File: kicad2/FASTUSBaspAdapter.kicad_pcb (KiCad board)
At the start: 2 copper layers, 73.7 x 29.2 mm, 2 parts, among them CON1 AVR-ISP-6, U1 stm32f103c8t6-module-china

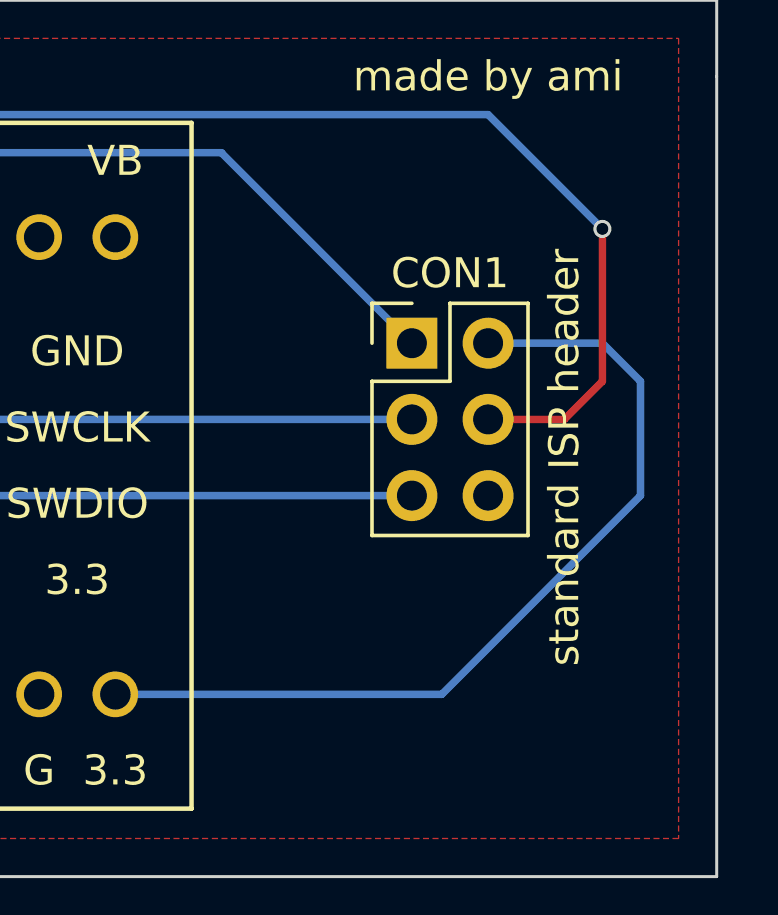
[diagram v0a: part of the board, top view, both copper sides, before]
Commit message: Add panelize pcb
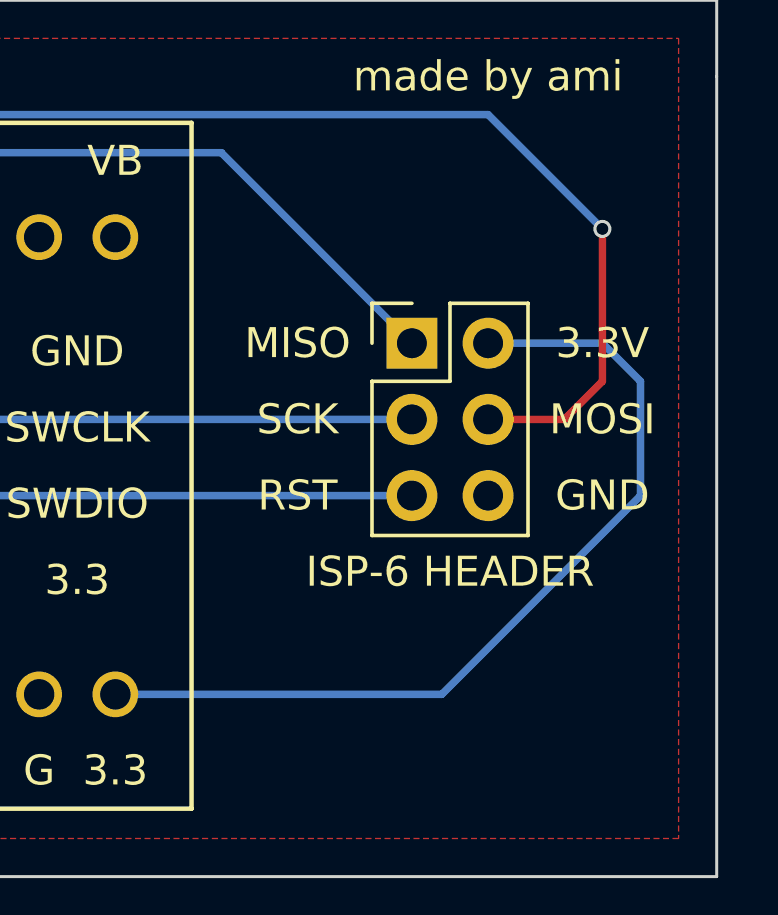
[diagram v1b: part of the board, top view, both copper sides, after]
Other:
- board text added: "3.3V"
- board text added: "GND"
- board text added: "ISP-6 HEADER"
- board text added: "MISO"
- board text added: "MOSI"
- board text added: "RST"
- board text added: "SCK"
- board text removed: "standard ISP header"
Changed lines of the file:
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@@
     (area 162.509999 101.549999 236.270001 130.860001)
     (thickness 1.6)
-    (drawings 9)
+    (drawings 15)
     (tracks 23)
     (zones 0)
@@
     (descr "Through hole straight pin header, 2x03, 2.54mm pitch, double rows")
     (tags "Through hole pin header THT 2x03 2.54mm double row")
-    (fp_text reference CON1 (at 1.27 -2.33) (layer F.SilkS)
-      (effects (font (size 1 1) (thickness 0.15)))
-    )
-    (fp_text value AVR-ISP-6 (at 1.27 7.41) (layer F.Fab)
+    (fp_text reference CON1 (at 1.27 -2.33) (layer F.SilkS) hide
+      (effects (font (size 1 1) (thickness 0.15)))
+    )
+    (fp_text value AVR-ISP-6 (at 1.27 7.41) (layer F.Fab) hide
       (effects (font (size 1 1) (thickness 0.15)))
     )
@@
     (fp_line (start 4.35 6.85) (end 4.35 -1.8) (layer F.CrtYd) (width 0.05))
     (fp_line (start 4.35 -1.8) (end -1.8 -1.8) (layer F.CrtYd) (width 0.05))
-    (fp_text user %R (at 1.27 -2.33) (layer F.Fab)
+    (fp_text user "ISP-6 HEADER" (at 1.27 -2.33) (layer F.Fab)
       (effects (font (size 1 1) (thickness 0.15)))
     )
@@
       (net 38 "Net-(U1-Pad40)"))
   )
-  (gr_text "standard ISP header" (at 231.14 116.84 90) (layer F.SilkS)
+  (gr_text GND (at 232.41 118.11) (layer F.SilkS)
+    (effects (font (size 1 1) (thickness 0.2)))
+  )
+  (gr_text MOSI (at 232.41 115.57) (layer F.SilkS)
+    (effects (font (size 1 1) (thickness 0.2)))
+  )
+  (gr_text 3.3V (at 232.41 113.03) (layer F.SilkS)
+    (effects (font (size 1 1) (thickness 0.2)))
+  )
+  (gr_text "ISP-6 HEADER" (at 227.33 120.65) (layer F.SilkS)
+    (effects (font (size 1 1) (thickness 0.1)))
+  )
+  (gr_text RST (at 222.25 118.11) (layer F.SilkS)
+    (effects (font (size 1 1) (thickness 0.2)))
+  )
+  (gr_text SCK (at 222.25 115.57) (layer F.SilkS)
+    (effects (font (size 1 1) (thickness 0.2)))
+  )
+  (gr_text MISO (at 222.25 113.03) (layer F.SilkS)
     (effects (font (size 1 1) (thickness 0.2)))
   )
@@
   (gr_line (start 236.22 130.81) (end 162.56 130.81) (angle 90) (layer Edge.Cuts) (width 0.1))
   (gr_line (start 236.22 104.14) (end 236.22 130.81) (angle 90) (layer Edge.Cuts) (width 0.1))
-  (segment (start 190.775001 109.495001) (end 190.775001 107.674999) (width 0.25) (layer B.Cu) (net 1) (status 400000))
-  (segment (start 219.71 106.68) (end 226.06 113.03) (width 0.25) (layer B.Cu) (net 1) (status 800000))
+  (segment (start 190.775001 109.495001) (end 190.775001 107.674999) (width 0.25) (layer B.Cu) (net 1))
+  (segment (start 219.71 106.68) (end 226.06 113.03) (width 0.25) (layer B.Cu) (net 1))
   (segment (start 191.77 106.68) (end 219.71 106.68) (width 0.25) (layer B.Cu) (net 1))
   (segment (start 190.775001 107.674999) (end 191.77 106.68) (width 0.25) (layer B.Cu) (net 1))
-  (segment (start 193.315001 109.495001) (end 193.315001 113.305001) (width 0.25) (layer B.Cu) (net 2) (status 400000))
-  (segment (start 195.58 115.57) (end 226.06 115.57) (width 0.25) (layer B.Cu) (net 2) (status 800000))
+  (segment (start 193.315001 109.495001) (end 193.315001 113.305001) (width 0.25) (layer B.Cu) (net 2))
+  (segment (start 195.58 115.57) (end 226.06 115.57) (width 0.25) (layer B.Cu) (net 2))
   (segment (start 193.315001 113.305001) (end 195.58 115.57) (width 0.25) (layer B.Cu) (net 2))
   (segment (start 188.235001 109.495001) (end 188.235001 107.674999) (width 0.25) (layer B.Cu) (net 3))
@@
   (segment (start 190.5 105.41) (end 228.6 105.41) (width 0.25) (layer B.Cu) (net 3))
   (segment (start 188.235001 107.674999) (end 190.5 105.41) (width 0.25) (layer B.Cu) (net 3))
-  (segment (start 178.075001 124.735001) (end 178.075001 122.914999) (width 0.25) (layer B.Cu) (net 4) (status 400000))
-  (segment (start 182.88 118.11) (end 226.06 118.11) (width 0.25) (layer B.Cu) (net 4) (status 800000))
+  (segment (start 178.075001 124.735001) (end 178.075001 122.914999) (width 0.25) (layer B.Cu) (net 4))
+  (segment (start 182.88 118.11) (end 226.06 118.11) (width 0.25) (layer B.Cu) (net 4))
   (segment (start 178.075001 122.914999) (end 182.88 118.11) (width 0.25) (layer B.Cu) (net 4))
-  (segment (start 216.175001 124.735001) (end 227.054999 124.735001) (width 0.25) (layer B.Cu) (net 39) (status 400000))
-  (segment (start 232.41 113.03) (end 228.6 113.03) (width 0.25) (layer B.Cu) (net 39) (status 800000))
+  (segment (start 216.175001 124.735001) (end 227.054999 124.735001) (width 0.25) (layer B.Cu) (net 39))
+  (segment (start 232.41 113.03) (end 228.6 113.03) (width 0.25) (layer B.Cu) (net 39))
   (segment (start 233.68 114.3) (end 232.41 113.03) (width 0.25) (layer B.Cu) (net 39))
   (segment (start 233.68 118.11) (end 233.68 114.3) (width 0.25) (layer B.Cu) (net 39))
